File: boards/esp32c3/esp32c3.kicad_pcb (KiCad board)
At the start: 2 copper layers, 32 x 46 mm, 21 parts, among them J1 USB-C, J2 IO, SW1 RESET, SW2 BOOT, U1 ESP32-C3-WROOM-02-N4, U2 AP2112K-3.3

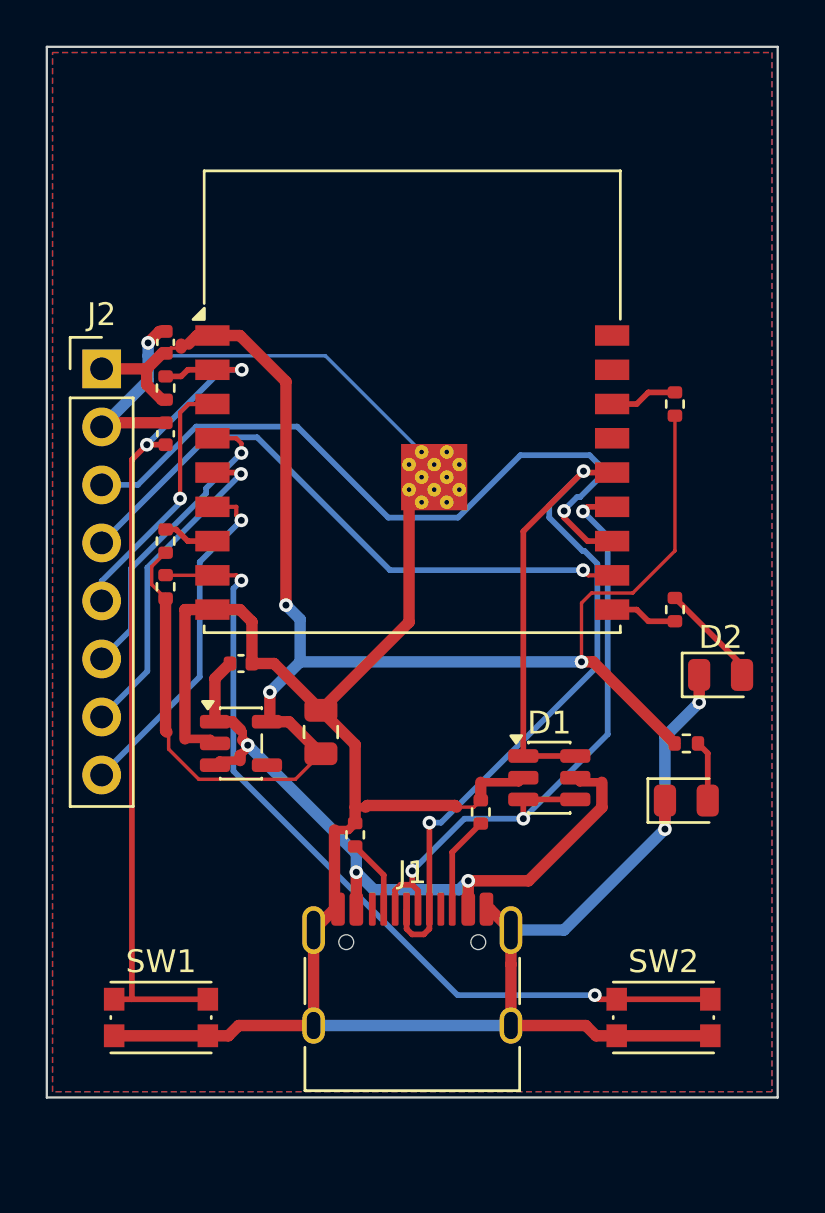
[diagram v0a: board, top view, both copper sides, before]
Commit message: esp32c3, relay8: LP38693 instead of AP2112K (hot-plug overshoot exceeded 6.5 V)
With only 1 uF on VBUS, cable ringing on hot-plug reaches 8.6 V (esp32c3) and
7.7 V (relay8, through SS34) at the LDO input; AP2112K's absolute maximum is
6.5 V. The USBLC6 VBUS zener lowers it by ~0.6 V, not enough. LP38693 is rated
12 V. New boards/esp32c3/sim/power_sim.py covers both boards and includes the
module's own ~12.3 uF (WROOM-02 datasheet fig. 8-1): total hot-plug charge is
~79 uC, over USB 2.0's 50 uC; documented as a compliance limitation.
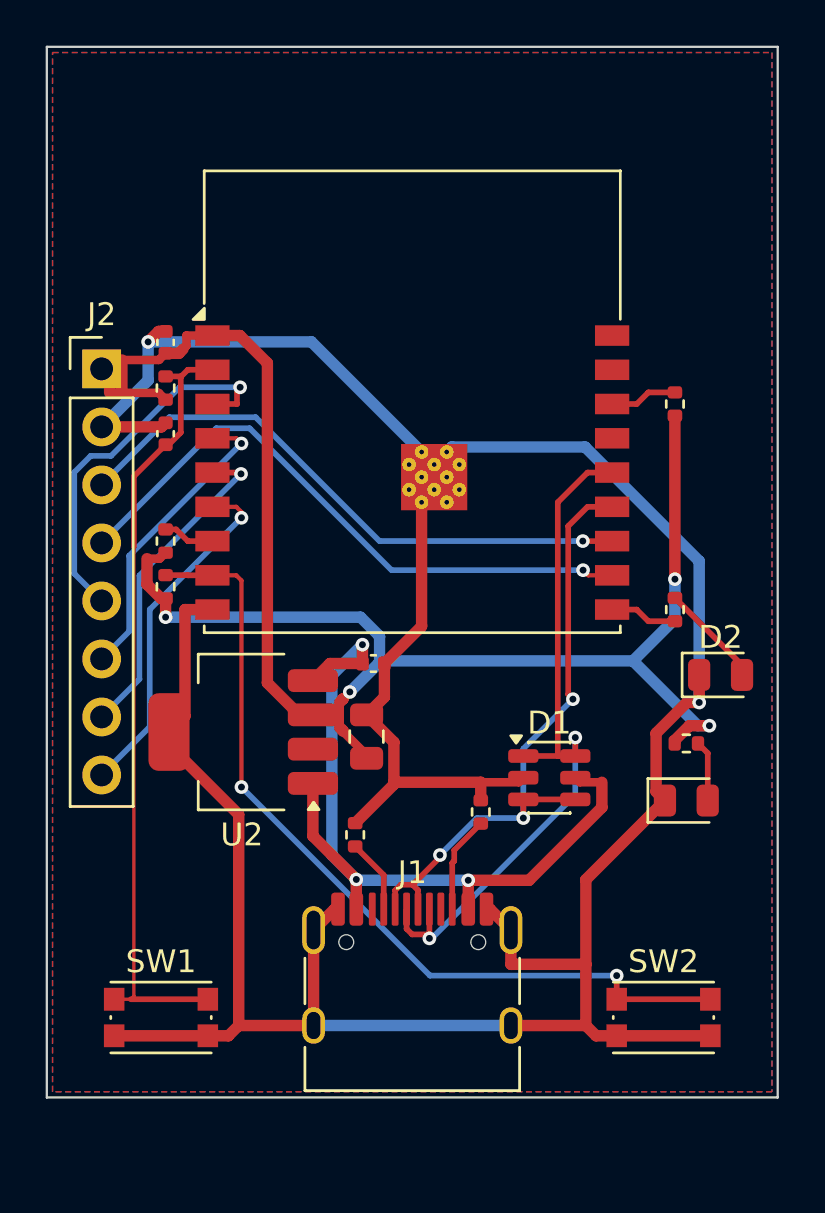
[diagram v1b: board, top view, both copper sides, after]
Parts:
- U2: value AP2112K-3.3 -> LP38693MP-3.3; footprint Package_TO_SOT_SMD:SOT-23-5 -> Package_TO_SOT_SMD:SOT-223-5
- moved C1 5.80 mm to (114.3, 127.0)
- moved C2 2.01 mm to (114.0, 130.2)
- moved U2 0.51 mm to (108.6, 130.0), turned to 180 degrees
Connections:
- U2 pad 2: GND -> unconnected-(U2-NC-Pad2)
- U2 pad 3: VBUS -> +3V3
- U2 pad 4: unconnected-(U2-NC-Pad4) -> VBUS
- U2 pad 5: +3V3 -> GND
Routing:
- net GND: track 131.5 -> 150.8 mm, vias 3 -> 2
- net USB_DP: track 44.1 -> 31.9 mm
- net IO4: track 11.2 -> 16.8 mm
- net TXD: track 31.3 -> 25.8 mm
- net VBUS: track 32.2 -> 36.6 mm
- net EN: track 38.4 -> 34.5 mm, vias 2 -> 0
- net +3V3: track 78.3 -> 79.8 mm, vias 3 -> 4
- net USB_DN: track 29.2 -> 28.1 mm
- net IO9: track 36.9 -> 37.4 mm

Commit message: esp32c3: VBUS soft-start (AO3401A) keeps hot-plug inrush within USB 2.0
The module's own ~12.3 uF plus C2 drew ~79 uC on hot-plug through the LDO
(limit 50 uC, i.e. a 10 uF-equivalent load). A P-MOSFET between VBUS and the
LDO with a gate RC (100k / 100nF gate-source / 10nF gate-drain) ramps the
output: simulated ramp current 80-97 mA (one unit load) over Vth -0.5..-1.3 V,
3V3 up in 1.3-3.7 ms. Board grows 46 -> 49 mm to fit it.

Also drop boards/relay8/terminals-closeup.png (v1 leftover, never tracked).
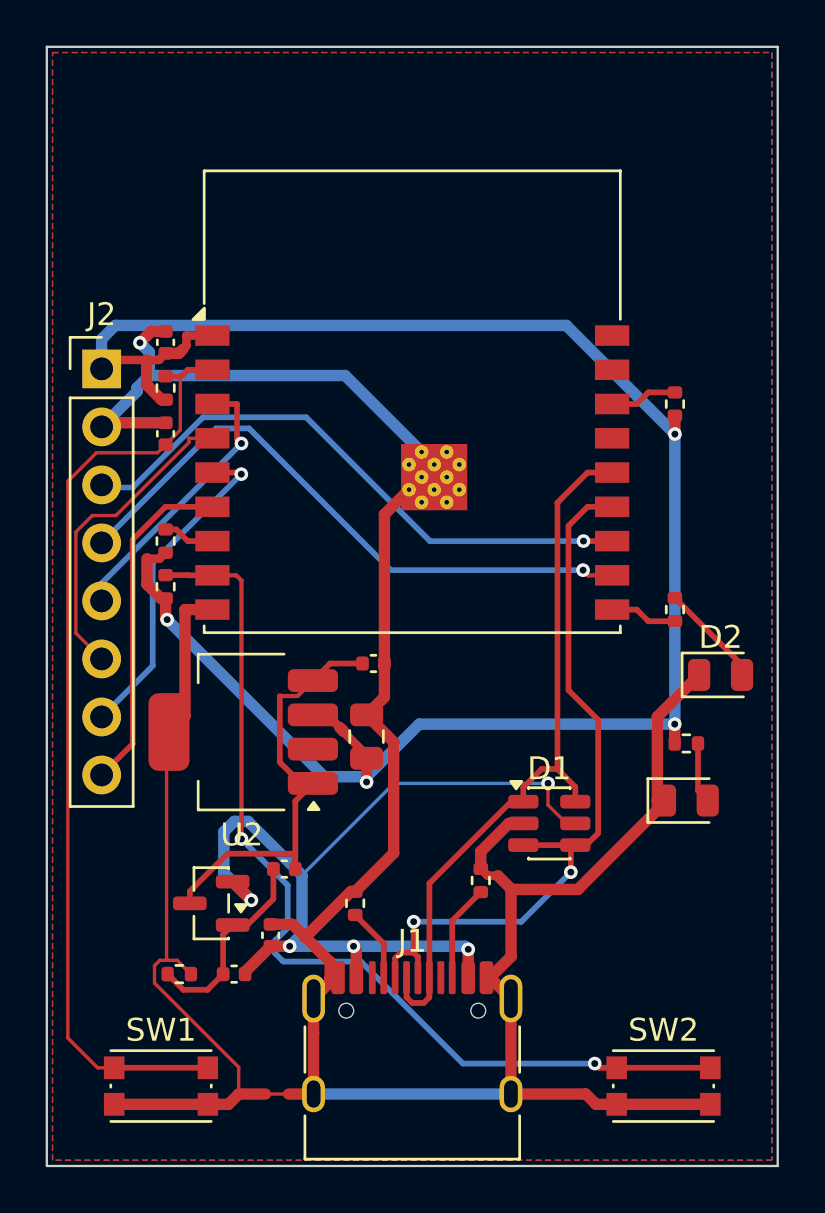
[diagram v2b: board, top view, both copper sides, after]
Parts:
- added C5: 1uF, Capacitor_SMD:C_0402_1005Metric, F.Cu at (114.3, 127.0)
- added C6: 100nF, Capacitor_SMD:C_0402_1005Metric, F.Cu at (108.2, 140.6)
- added C7: 10nF, Capacitor_SMD:C_0402_1005Metric, F.Cu at (110.4, 136.0)
- added Q1: AO3401A, Package_TO_SOT_SMD:SOT-23, F.Cu at (107.2, 137.5)
- added R9: 100k, Resistor_SMD:R_0402_1005Metric, F.Cu at (105.8, 140.6)
- moved C1 12.7 mm to (109.8, 138.9), turned to 90 degrees
- moved J1 3.00 mm to (116.0, 144.8)
- moved R1 3.00 mm to (113.5, 137.5)
- moved R2 3.00 mm to (119.0, 136.5)
- moved SW1 3.00 mm to (105.0, 145.5)
- moved SW2 3.00 mm to (127.0, 145.5)
- moved D1 2.00 mm to (122.0, 134.0)
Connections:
- U2 pad 1: VBUS -> VSW
- U2 pad 4: VBUS -> VSW
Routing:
- net VSW: track 0.00 -> 18.7 mm
- net SS_G: track 0.00 -> 8.88 mm
- net EN: track 34.5 -> 41.4 mm
- net +3V3: track 79.8 -> 85.5 mm
- net GND: track 150.8 -> 145.4 mm, vias 2 -> 1
- net USB_DN: track 28.1 -> 33.0 mm, vias 3 -> 2
- net IO9: track 37.4 -> 41.9 mm
- net IO4: track 16.8 -> 12.3 mm
- net VBUS: track 36.6 -> 40.5 mm, vias 3 -> 5
- net IO5: track 13.3 -> 13.8 mm, vias 1 -> 0
- net IO7: track 15.4 -> 15.0 mm, vias 1 -> 0
- net USB_DP: track 31.9 -> 31.5 mm, vias 2 -> 0
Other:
- board size 32 x 46 mm -> 32 x 49 mm

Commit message: fab: Gerber/drill zip + JLCPCB BOM/CPL with self-checks; USBLC6-2SC6 to match SOT-23-6
lib/fab.py runs as the last build step on all three boards. It refuses to
write the zip when a required Gerber layer is missing or empty, when the
drill-hit count differs from vias + plated/NPTH pad holes (route-format
slots counted once), or when BOM / CPL / board refdes sets disagree.

It also compares each symbol's library default footprint with the one
actually assigned. That caught all three boards using the USBLC6-2P6
symbol (SOT-666) on a SOT-23-6 footprint: electrically identical pinout,
so ERC/DRC/netlist checks passed, but a BOM ordered by value would buy a
part that does not fit. Switched to USBLC6-2SC6.

LCSC part numbers come from a hand-checked boards/<b>/lcsc.json; the
script never guesses them and lists missing rows in fab/missing-lcsc.txt.
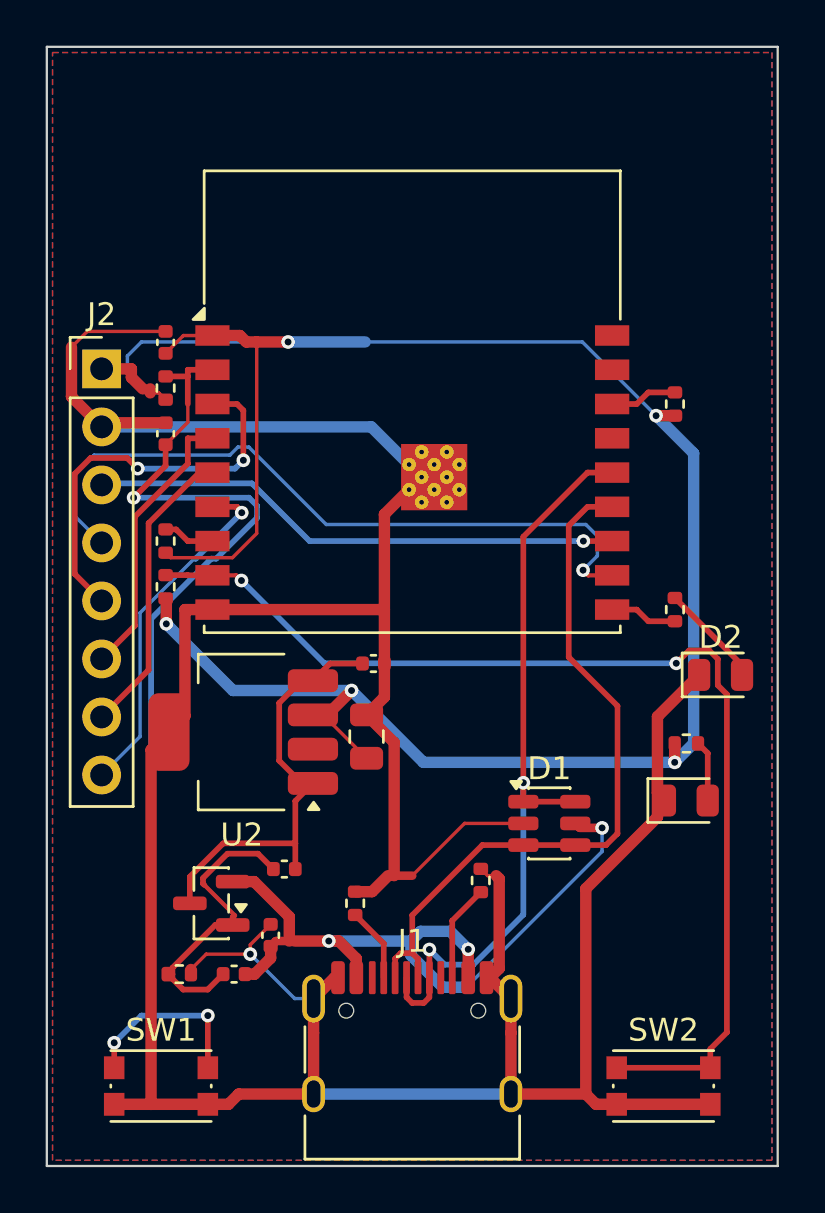
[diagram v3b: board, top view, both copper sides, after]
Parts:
- D1: value USBLC6-2P6 -> USBLC6-2SC6
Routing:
- net GND: track 145.4 -> 165.1 mm
- net +3V3: track 85.5 -> 97.8 mm, vias 4 -> 5
- net VBUS: track 40.5 -> 33.3 mm, vias 5 -> 3
- net IO9: track 41.9 -> 48.6 mm
- net IO4: track 12.3 -> 17.7 mm, vias 1 -> 2
- net EN: track 41.4 -> 46.5 mm, vias 0 -> 3
- net RXD: track 27.1 -> 31.6 mm
- net SS_G: track 8.88 -> 13.3 mm
- net USB_DP: track 31.5 -> 34.2 mm, vias 0 -> 2
- net TXD: track 25.9 -> 23.4 mm
- net IO5: track 13.8 -> 12.3 mm
- net IO6: track 14.5 -> 13.0 mm, vias 1 -> 0
- net USB_DN: track 33.0 -> 31.6 mm, vias 2 -> 0
- net IO7: track 15.0 -> 15.5 mm, vias 0 -> 1

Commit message: fab: verified LCSC part numbers for all three boards; BOM/CPL ready to upload
lib/lcsc.py checks every hand-written part number in boards/<b>/lcsc.json
against the JLCPCB parts API: the part exists, its model equals the one
written down, stock covers 5 boards, the package matches what the KiCad
footprint name implies (0402/0805, SOT-23(-6), SOT-223-5, SMA, SOIC-W,
CP_Elec, 2.54 mm headers), resistor/capacitor values match the JLC
attributes and LED colours match. A mutation test (1k part for a 10k
resistor, wrong model, 0805 part on a 0402 footprint, missing row) fails
all four. Results go to lcsc-check.json with a hash of lcsc.json, so the
build itself stays offline and refuses a stale check.

fab.py now writes BOM/CPL only for assembled parts, lists parts LCSC
cannot supply in hand-solder.csv (relay8: mains terminals and fuse
holders), applies lib/jlc_rotations.json to the CPL and writes
rotation-review.csv. None of the rotation corrections are verified on
hardware; every row says so.
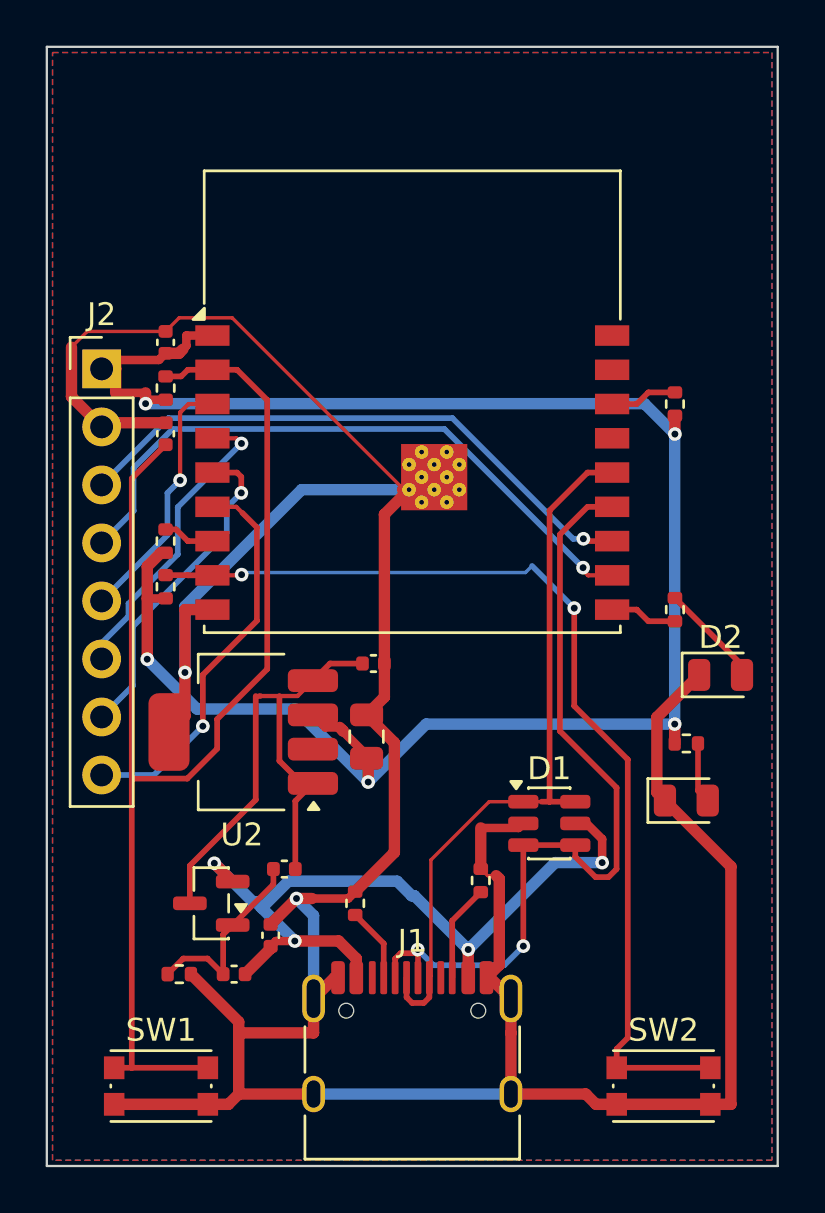
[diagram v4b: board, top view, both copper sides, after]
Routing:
- net +3V3: track 97.8 -> 84.4 mm
- net EN: track 46.5 -> 57.6 mm, vias 3 -> 0
- net IO4: track 17.7 -> 11.2 mm, vias 2 -> 1
- net GND: track 165.1 -> 159.9 mm, vias 1 -> 2
- net VSW: track 19.1 -> 24.2 mm
- net USB_DN: track 31.6 -> 36.4 mm, vias 0 -> 2
- net SS_G: track 13.3 -> 8.51 mm
- net IO9: track 48.6 -> 44.2 mm
- net RXD: track 31.6 -> 28.2 mm
- net USB_DP: track 34.2 -> 31.7 mm, vias 2 -> 0
- net TXD: track 23.4 -> 25.8 mm
- net IO7: track 15.5 -> 17.3 mm
- net VBUS: track 33.3 -> 34.7 mm, vias 3 -> 4
- net IO6: track 13.0 -> 14.4 mm, vias 0 -> 1
- net IO5: track 12.3 -> 13.3 mm, vias 0 -> 1

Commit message: review: datasheet design review on the netlist; fixes a reversed TVS and dim LEDs
lib/review.py checks the design intent that ERC and the netlist check take
on trust: diode/TVS polarity against inferred rail voltages, LED current
from the JLC Vf range, per-datasheet decoupling and supply ranges, USB-C
CC pull-downs and D+/D- on both sides, ESP32-C3 EN RC, strapping pins and
GPIO18/19, relay flyback path and pickup voltage, capacitor rating and
polarity. It runs after the netlist check and stops the build on ERROR.
lib/review_test.py breaks the real netlists 15 ways; every rule fires and
the unmodified boards report no ERROR.

Real defects it found:
- usbc-ldo: SMAJ5.0A had anode on +5V and cathode on GND (KiCad names
  the cathode pin "A1"), shorting the rail on plug-in. Swapped.
- esp32c3: blue user LED on a 3.3 V GPIO (Vf 2.5-3.6 V) -> yellow, 470R.
- esp32c3, relay8: green power LED at ~0.45 mA through 1k -> 220R.
- usbc-ldo: SS32 symbol for an SS34 part -> Diode:SS34.

Also: lcsc-check.json keeps JLC attributes (Vf, voltage rating) for the
review; lcsc.py groups parts from net.txt instead of fab/groups.json; the
build retries freerouting (up to 3 runs) because it is not deterministic
and occasionally leaves two connections unrouted on the same DSN.
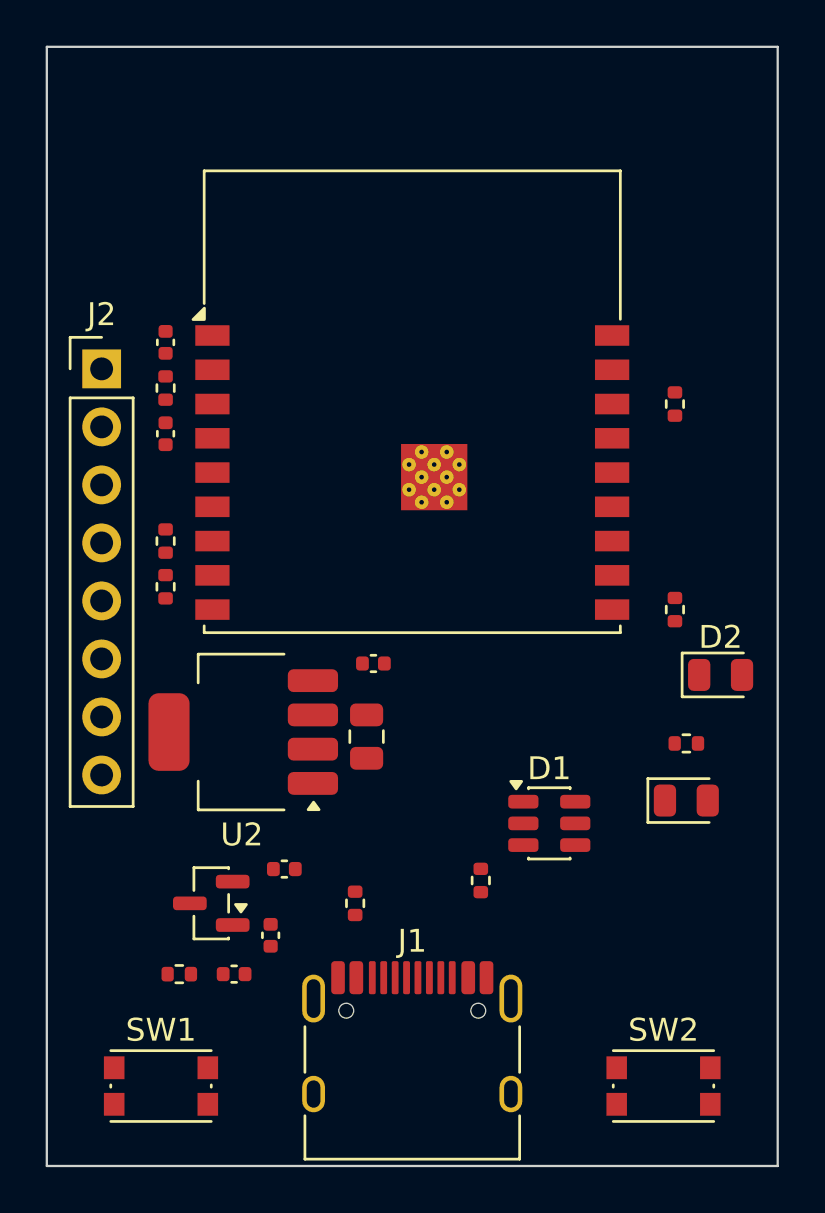
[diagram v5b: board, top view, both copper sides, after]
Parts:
- D2: value BLUE -> KT-0805Y
- R7: value 1k -> 470
- R8: value 1k -> 220
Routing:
- net GND: track 159.9 -> 0.00 mm, vias 2 -> 0
- net +3V3: track 84.4 -> 0.00 mm, vias 5 -> 0
- net EN: track 57.6 -> 0.00 mm
- net IO9: track 44.2 -> 0.00 mm, vias 2 -> 0
- net USB_DN: track 36.4 -> 0.00 mm, vias 2 -> 0
- net VBUS: track 34.7 -> 0.00 mm, vias 4 -> 0
- net USB_DP: track 31.7 -> 0.00 mm
- net RXD: track 28.2 -> 0.00 mm, vias 1 -> 0
- net TXD: track 25.8 -> 0.00 mm, vias 1 -> 0
- net VSW: track 24.2 -> 0.00 mm
- net IO7: track 17.3 -> 0.00 mm, vias 1 -> 0
- net IO6: track 14.4 -> 0.00 mm, vias 1 -> 0
- net IO5: track 13.3 -> 0.00 mm, vias 1 -> 0
- net IO4: track 11.2 -> 0.00 mm, vias 1 -> 0
- net SS_G: track 8.51 -> 0.00 mm
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- removed copper zone on B.Cu, net GND
- removed copper zone on F.Cu, net GND
